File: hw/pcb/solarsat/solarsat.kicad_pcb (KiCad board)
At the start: 2 copper layers, 20 x 20 mm, 28 parts, among them J1 Conn_01x01, J10 Conn_01x01, J11 Conn_01x01, J12 Conn_01x01, J13 Conn_01x01, J2 Conn_02x03_Odd_Even, J3 Conn_01x01, J4 Conn_01x01, J5 Conn_01x01, J6 Conn_01x01, J7 Conn_01x01, J8 Conn_01x01, J9 Conn_01x01, U1 SPV1050

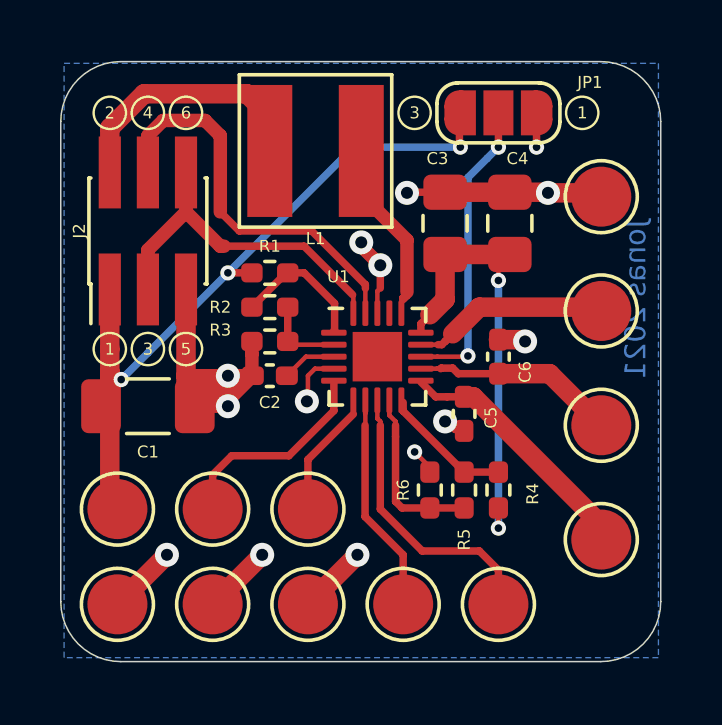
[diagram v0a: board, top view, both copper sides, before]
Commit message: connect spv1050 pad to gnd
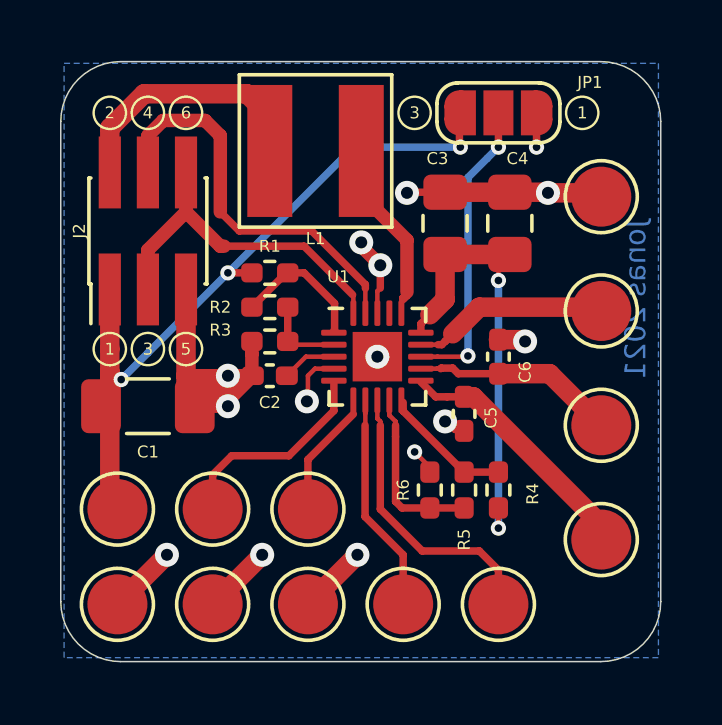
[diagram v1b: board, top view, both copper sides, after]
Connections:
- U1 pad 21: (no net) -> GND
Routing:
- net GND: vias 14 -> 15

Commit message: rework layout: shield dcdc better
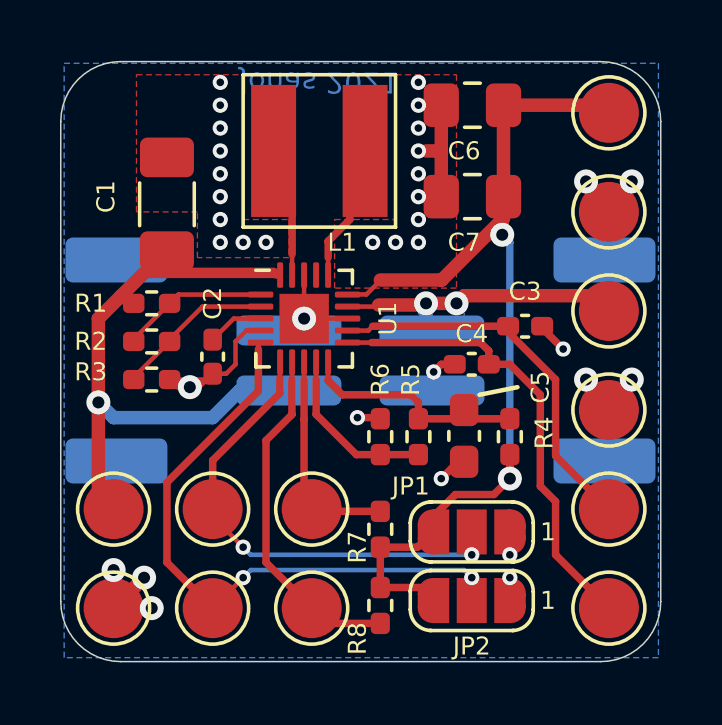
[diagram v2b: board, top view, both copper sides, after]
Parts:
- added C7: 22u, Capacitor_SMD:C_0805_2012Metric_Pad1.18x1.45mm_HandSolder, F.Cu at (139.7, 79.5)
- added J14: Conn_01x02, Connector_JST:JST_PH_S2B-PH-SM4-TB_1x02-1MP_P2.00mm_Horizontal, B.Cu at (141.2, 85.0)
- added JP2: SolderJumper_3_Open, Jumper:SolderJumper-3_P1.3mm_Open_RoundedPad1.0x1.5mm_NumberLabels, F.Cu at (139.7, 93.0)
- added R7: 10M, Resistor_SMD:R_0402_1005Metric_Pad0.72x0.64mm_HandSolder, F.Cu at (136.7, 90.6)
- added R8: 10M, Resistor_SMD:R_0402_1005Metric_Pad0.72x0.64mm_HandSolder, F.Cu at (136.7, 93.1)
- C3, C4: value C -> 100n; footprint Capacitor_SMD:C_0805_2012Metric_Pad1.18x1.45mm_HandSolder -> Capacitor_SMD:C_0402_1005Metric_Pad0.74x0.62mm_HandSolder
- C5: value 100n -> 470n; footprint Capacitor_SMD:C_0402_1005Metric_Pad0.74x0.62mm_HandSolder -> Capacitor_SMD:C_0603_1608Metric_Pad1.08x0.95mm_HandSolder
- C6: value 100n -> 22u; footprint Capacitor_SMD:C_0402_1005Metric_Pad0.74x0.62mm_HandSolder -> Capacitor_SMD:C_0805_2012Metric_Pad1.18x1.45mm_HandSolder
- J13: value Conn_01x01 -> Conn_01x02; footprint TestPoint:TestPoint_Pad_D2.0mm -> Connector_JST:JST_PH_S2B-PH-SM4-TB_1x02-1MP_P2.00mm_Horizontal; moved to B.Cu
- J2: value Conn_02x03_Odd_Even -> Conn_01x01; footprint Connector_PinHeader_1.27mm:PinHeader_2x03_P1.27mm_Vertical_SMD -> TestPoint:TestPoint_Pad_D2.0mm
- JP1: value Jumper_NC_Dual -> SolderJumper_3_Open
- R2: value R -> 0M59
- R3: value R -> 2M49
- R5: value R -> 1M2
- R6: value R -> 4M7
- moved J9 18.9 mm to (131.1, 93.2)
- moved J5 17.4 mm to (127.8, 93.2)
- moved J4 16.6 mm to (144.3, 76.7)
- moved J2 15.4 mm to (144.3, 80.0)
- moved JP1 14.0 mm to (139.7, 90.7)
- moved J6 13.2 mm to (144.3, 89.9)
- moved J7 10.0 mm to (131.1, 89.9)
- moved J13 8.62 mm to (130.8, 85.0), turned to 90 degrees
- moved C6 8.43 mm to (139.7, 76.5), turned to 180 degrees
- moved J3 7.62 mm to (144.3, 83.3)
- moved J8 6.86 mm to (144.3, 93.2)
- moved C1 6.76 mm to (129.5, 79.8), turned to 90 degrees
- moved C4 4.87 mm to (139.7, 85.1), turned to 180 degrees
- moved J10 4.58 mm to (134.4, 89.9)
- moved C3 4.34 mm to (141.5, 83.8), turned to 0 degrees
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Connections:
- C3 pad 1: Net-(C3-Pad1) -> /LDO2_3V3
- C4 pad 1: Net-(C3-Pad1) -> /LDO1_1V8
- C5 pad 1: /LDO1 -> Net-(C5-Pad1)
- C6 pad 1: /LDO2 -> /STORE
- J10 pad 1: GND -> /~BAT_CON
- J11 pad 1: GND -> /~BAT_CHG
- J12 pad 1: +BATT -> GND
- J13 pad 1: GND -> VBUS
- J2 pad 1: VBUS -> GND
- J3 pad 1: /LDO1 -> +BATT
- J4 pad 1: Net-(J4-Pad1) -> /STORE
- J5 pad 1: /LDO2 -> GND
- J6 pad 1: Net-(J6-Pad1) -> /LDO2_3V3
- J7 pad 1: Net-(J7-Pad1) -> /LDO2_EN
- J8 pad 1: Net-(J8-Pad1) -> /LDO1_1V8
- J9 pad 1: GND -> /LDO1_EN
- JP1 pad 2: Net-(JP1-Pad2) -> /LDO2_EN
- JP1 pad 3: VBUS -> /STORE
- L1 pad 1: Net-(J2-Pad2) -> Net-(L1-Pad1)
- R4 pad 1: Net-(C3-Pad1) -> /STORE
- R4 pad 2: Net-(R4-Pad2) -> Net-(C5-Pad1)
- R5 pad 1: Net-(R4-Pad2) -> Net-(C5-Pad1)
- U1 pad 10: Net-(R4-Pad2) -> Net-(C5-Pad1)
- U1 pad 11: /LDO1 -> /LDO1_1V8
- U1 pad 12: /LDO2 -> /LDO2_3V3
- U1 pad 13: Net-(JP1-Pad2) -> GND
- U1 pad 15: Net-(C3-Pad1) -> /STORE
- U1 pad 17: Net-(U1-Pad17) -> (no net)
- U1 pad 19: Net-(J2-Pad4) -> Net-(L1-Pad1)
- U1 pad 20: Net-(J2-Pad3) -> VBUS
- U1 pad 5: Net-(J6-Pad1) -> /LDO1_EN
- U1 pad 6: Net-(J4-Pad1) -> /LDO2_EN
- U1 pad 7: Net-(J8-Pad1) -> /~BAT_CHG
- U1 pad 8: Net-(J7-Pad1) -> /~BAT_CON
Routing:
- net /STORE: track 0.00 -> 33.4 mm, vias 0 -> 2
- net /LDO1_EN: track 0.00 -> 20.8 mm, vias 0 -> 2
- net /LDO2_EN: track 0.00 -> 16.0 mm, vias 0 -> 2
- net /LDO1_1V8: track 0.00 -> 16.0 mm
- net Net-(C3-Pad1): track 15.1 -> 0.00 mm, vias 2 -> 0
- net Net-(J2-Pad4): track 13.4 -> 0.00 mm
- net /LDO2_3V3: track 0.00 -> 12.9 mm
- net Net-(J2-Pad3): track 11.7 -> 0.00 mm
- net /~BAT_CHG: track 0.00 -> 11.7 mm
- net Net-(JP1-Pad2): track 10.1 -> 0.00 mm, vias 2 -> 0
- net Net-(J7-Pad1): track 10.1 -> 0.00 mm
- net /LDO1: track 8.91 -> 0.00 mm
- net Net-(J2-Pad2): track 8.74 -> 0.00 mm
- net Net-(J6-Pad1): track 8.72 -> 0.00 mm
- net Net-(J8-Pad1): track 7.77 -> 0.00 mm
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- added copper zone on B.Cu, net +BATT
- added copper zone on F.Cu, net GND
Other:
- board text removed: "+BATT"
- board text removed: "1"
- board text removed: "2"
- board text removed: "3"
- board text removed: "4"
- board text removed: "5"
- board text removed: "6"
- board text removed: "GND"
- board text removed: "LDO1 1.8 V"
- board text removed: "LDO1 EN"
- board text removed: "LDO2 3.3 V"
- board text removed: "LDO2 EN"
- board text removed: "VBUS"
- board text removed: "~CHG"
- board text removed: "~CONN"

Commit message: add more shielding and another input cap, overkill is king
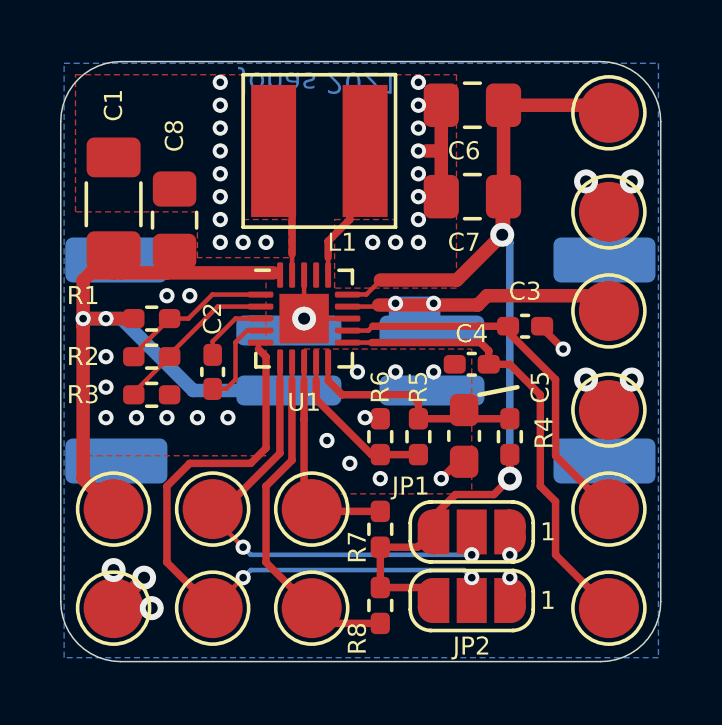
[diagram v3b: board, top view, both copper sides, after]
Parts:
- added C8: NC, Capacitor_SMD:C_0805_2012Metric_Pad1.18x1.45mm_HandSolder, F.Cu at (129.8, 80.3)
- moved C1 1.78 mm to (127.8, 79.8)
- moved C2 0.51 mm to (131.1, 85.3)
- moved R1 0.51 mm to (129.0, 83.6)
- moved R2 0.51 mm to (129.0, 84.8)
- moved R3 0.51 mm to (129.0, 86.1)
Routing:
- net VBUS: track 21.5 -> 27.5 mm, vias 1 -> 2
- net +BATT: track 10.8 -> 16.1 mm
- net GND: track 27.6 -> 24.4 mm, vias 35 -> 48
- net /LDO1_EN: track 20.8 -> 22.2 mm
- removed copper zone on B.Cu, net +BATT
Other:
- board text added: "2.6V<Voc<18V"
- board text added: "BATTERY"
- board text added: "LiPo 3.7 V"
- board text added: "SOLAR"

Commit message: increase size of store caps to 1206, and other smaller tweaks
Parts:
- C6, C7: footprint Capacitor_SMD:C_0805_2012Metric_Pad1.18x1.45mm_HandSolder -> Capacitor_SMD:C_1206_3216Metric_Pad1.33x1.80mm_HandSolder
- moved C7 0.55 mm to (140.2, 79.8)
- moved C6 0.49 mm to (140.2, 76.5)
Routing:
- net VBUS: track 27.5 -> 29.8 mm
- net GND: track 24.4 -> 22.3 mm
- net /STORE: track 33.7 -> 31.7 mm
- net /LDO1_1V8: track 16.0 -> 17.0 mm
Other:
- board text added: "LiPo 3.7V"
- board text removed: "LiPo 3.7 V"

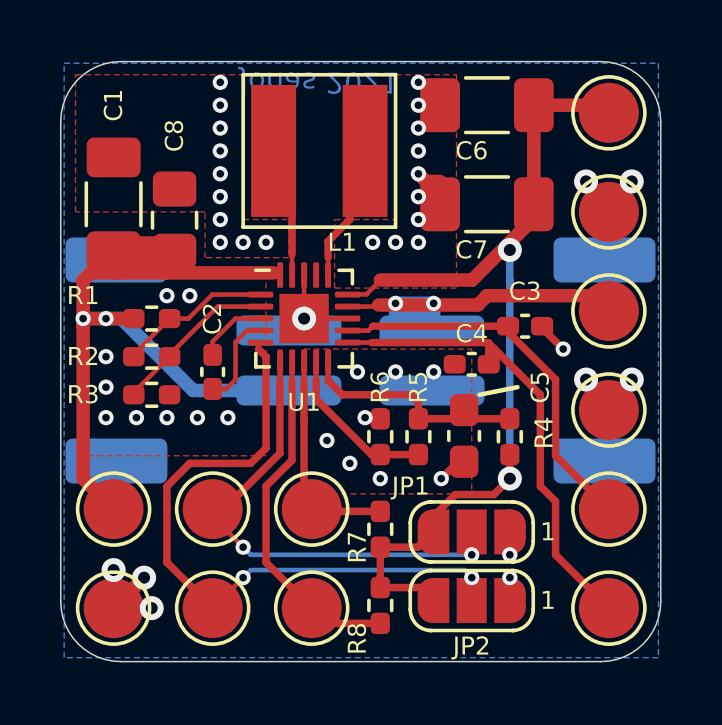
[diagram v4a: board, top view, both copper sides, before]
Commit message: connect signal ground pin 4 directly to exposed pad gnd as per reference design
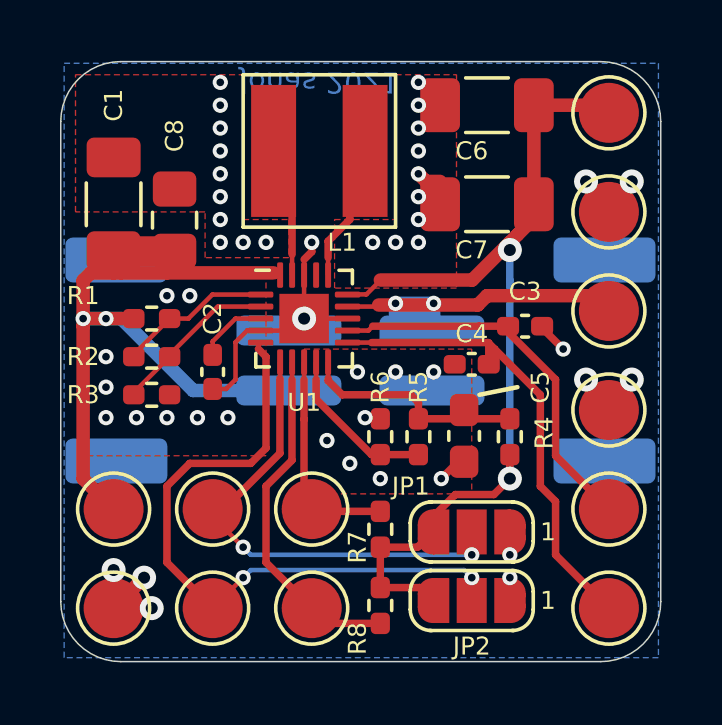
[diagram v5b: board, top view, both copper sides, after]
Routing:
- net GND: track 22.3 -> 24.6 mm, vias 48 -> 49

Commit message: removed ldo for 1.8 V
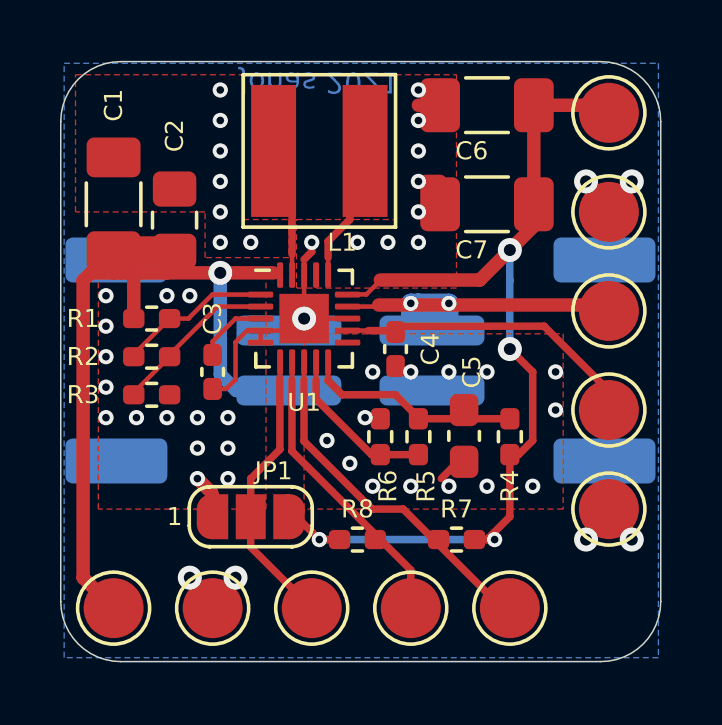
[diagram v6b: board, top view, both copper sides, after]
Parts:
- removed the C2 at (131.1, 85.3)
- removed the C4 at (139.7, 85.1)
- removed the J5 at (127.8, 93.2)
- removed the J8 at (144.3, 93.2)
- removed the J9 at (131.1, 93.2)
- removed JP2: SolderJumper_3_Open, Jumper:SolderJumper-3_P1.3mm_Open_RoundedPad1.0x1.5mm_NumberLabels
- added C3: 10n, Capacitor_SMD:C_0402_1005Metric_Pad0.74x0.62mm_HandSolder, F.Cu at (131.1, 85.3)
- added J7: Conn_01x01, TestPoint:TestPoint_Pad_D2.0mm, F.Cu at (131.1, 93.2)
- C2: renamed from C8; value NC -> DNM
- moved J10 7.38 mm to (141.0, 93.2)
- moved JP1 7.38 mm to (132.3, 90.2), turned to 0 degrees
- moved J9 4.67 mm to (134.4, 93.2)
- moved C4 4.38 mm to (137.2, 84.6), turned to 270 degrees
- moved J1 3.30 mm to (127.8, 93.2)
- moved J11 3.30 mm to (137.7, 93.2)
- moved J12 3.30 mm to (144.3, 89.9)
- moved J8 3.30 mm to (144.3, 86.6)
- moved R7 2.56 mm to (139.2, 90.9), turned to 180 degrees
- moved R8 2.32 mm to (135.9, 90.9), turned to 0 degrees
- renumbered C3 to C4, J13 to J2, J2 to J3, J14 to J4, J3 to J5, J4 to J6, J6 to J8, J7 to J9
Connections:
- U1 pad 11: /LDO1_1V8 -> (no net)
- U1 pad 5: /LDO1_EN -> GND
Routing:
- net /LDO1_EN: track 22.2 -> 0.00 mm, vias 2 -> 0
- net /LDO1_1V8: track 17.0 -> 0.00 mm
- net /LDO2_EN: track 16.2 -> 9.45 mm, vias 2 -> 0
- net /~BAT_CON: track 7.32 -> 11.9 mm
- net +BATT: track 16.1 -> 13.0 mm
- net GND: track 24.6 -> 22.0 mm, vias 49 -> 52
- net /LDO2_3V3: track 12.9 -> 10.3 mm
- net /STORE: track 31.7 -> 33.5 mm, vias 2 -> 4
- net /~BAT_CHG: track 11.7 -> 9.94 mm
- net VBUS: track 29.8 -> 30.3 mm, vias 2 -> 1
